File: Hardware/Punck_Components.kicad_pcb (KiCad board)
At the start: 4 copper layers, 91.2 x 99.8 mm, 115 parts, among them J1 Conn_01x12_Female, J2 Conn_01x12_Female, J3 Conn_01x12_Female, J4 Conn_01x12_Female, J5 Debug_Header, J6 SWD_Header, J7 Eurorack_10_pin_power, Q1 MMBT3904, Q2 MMBT3904, Q3 MMBT3904, Q4 MMBT3904, Q5 MMBT3904, Q6 MMBT3904, Q7 MMBT3904, U1 TL074, U2 STM32H743ZITx, U3 W25Q128JVS, U4 PCM5100APW, U5 W25Q128JVS, U6 TPS561201, U7 LD1117-3.3-4Tab, Y1 8MHz 20pF

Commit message: More PCB tweaking
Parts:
- moved R19 2.60 mm to (149.6, 119.6)
- moved R21 2.60 mm to (149.6, 122.2)
- moved R22 2.40 mm to (149.6, 124.8)
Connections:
- J2 pad 11: unconnected-(J2-Pad11) -> /TEMPO_OUT
- J4 pad 1: GND -> /USB_DP
- J4 pad 10: /TEMPO_OUT -> /AUDIO_OUT_L
- J4 pad 2: /USB_DP -> /USB_DM
- J4 pad 3: /USB_DM -> /USB_VBUS
- J4 pad 4: /USB_VBUS -> /KI_LED
- J4 pad 5: /KI_LED -> /SN_LED
- J4 pad 6: /SN_LED -> /HH_LED
- J4 pad 7: /HH_LED -> /SEQ_SELECT
- J4 pad 8: /SEQ_SELECT -> GND
- J4 pad 9: /AUDIO_OUT_L -> GND
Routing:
- net /TEMPO_OUT: track 31.4 -> 78.2 mm, vias 0 -> 1
- net /HH_LED_OUT: track 42.8 -> 41.3 mm
- net /USB_DP: track 43.9 -> 42.8 mm
- net /KI_LED_OUT: track 39.1 -> 38.0 mm
- net /SN_LED_OUT: track 40.7 -> 39.7 mm
- net /SEQ_SELECT: track 54.3 -> 53.2 mm
- net /AUDIO_OUT_L: track 44.6 -> 45.6 mm
- net /USB_DM: track 45.6 -> 44.6 mm
- net /USB_VBUS: track 47.5 -> 46.6 mm

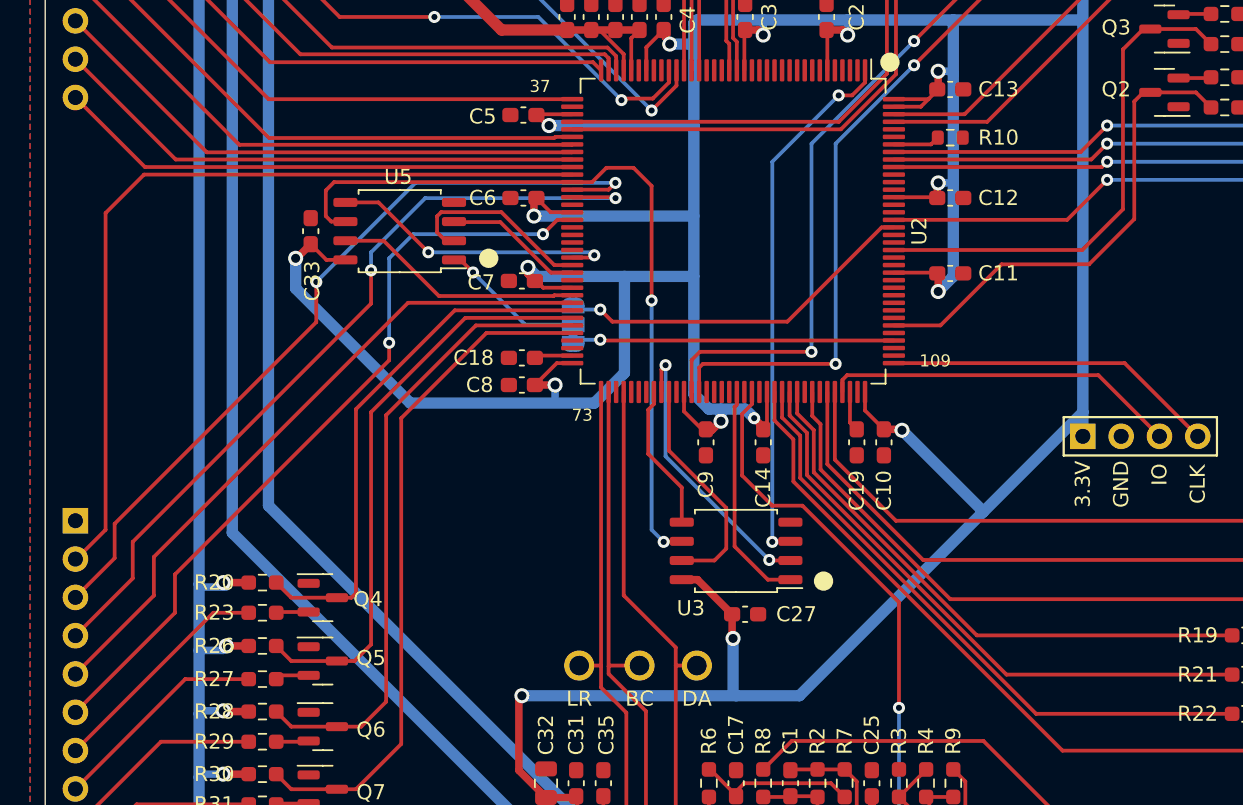
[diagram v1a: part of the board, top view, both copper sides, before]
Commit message: Added Logo to panel
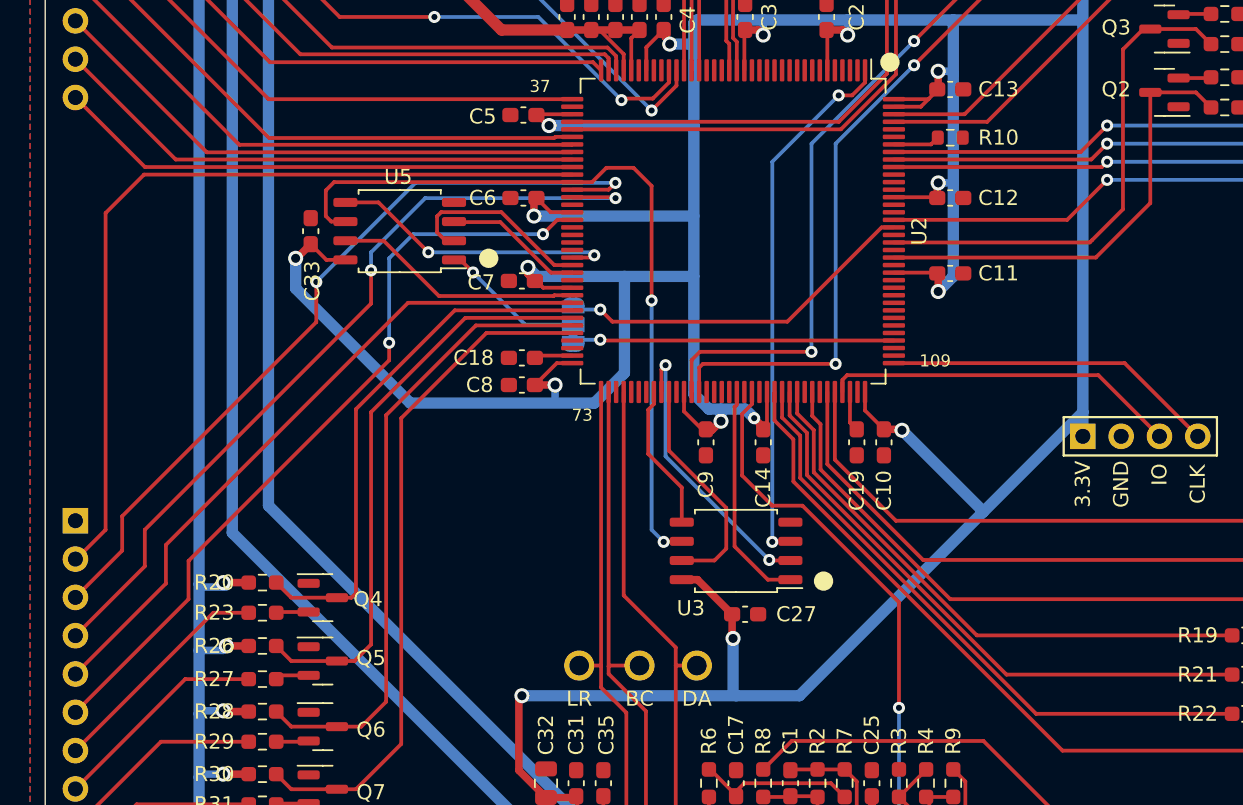
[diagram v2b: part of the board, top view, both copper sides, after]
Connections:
- U2 pad 114: /KICK_CLAMP -> unconnected-(U2-Pad114)
- U2 pad 123: unconnected-(U2-Pad123) -> /KICK_CLAMP
- U2 pad 124: /SNARE_CLAMP -> unconnected-(U2-Pad124)
- U2 pad 125: unconnected-(U2-Pad125) -> /SNARE_CLAMP
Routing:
- net /KICK_CLAMP: track 34.5 -> 32.4 mm

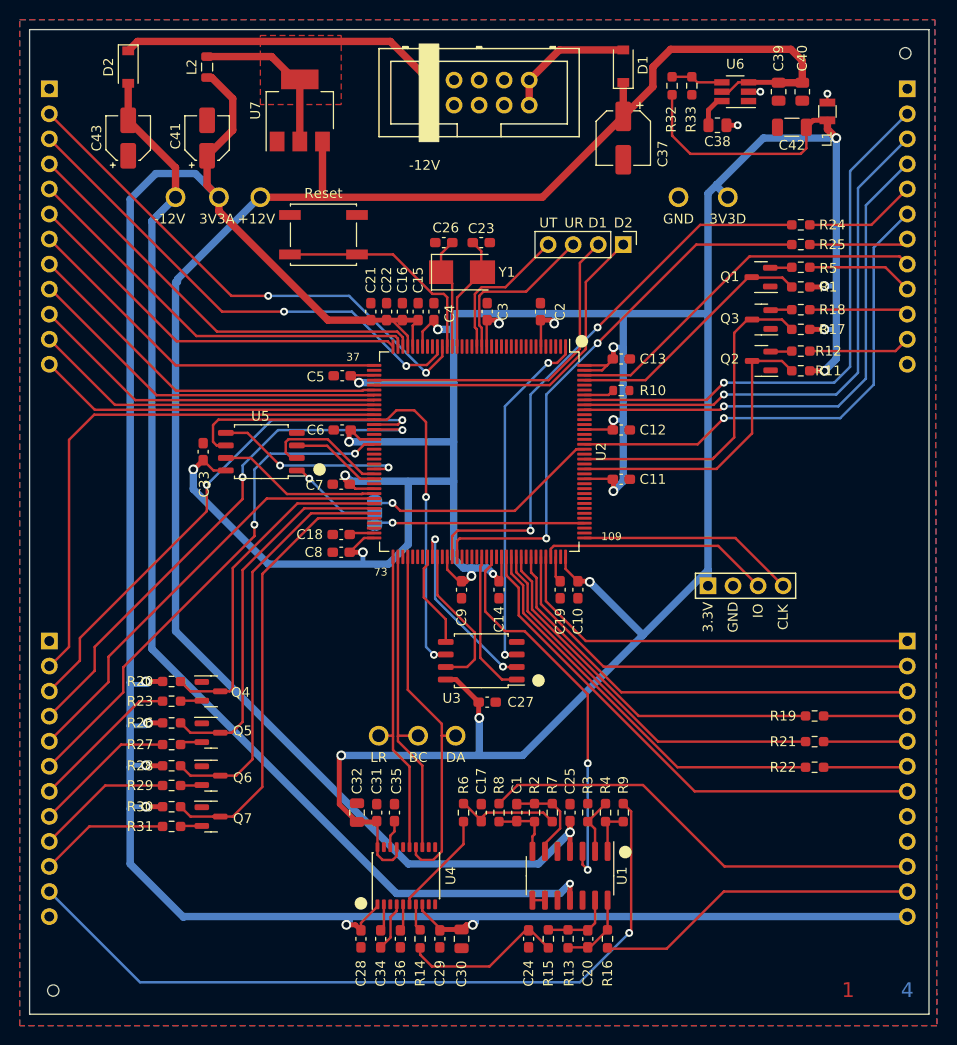
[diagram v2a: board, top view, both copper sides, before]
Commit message: More PCB tweaks; rejigged bottom row of controls
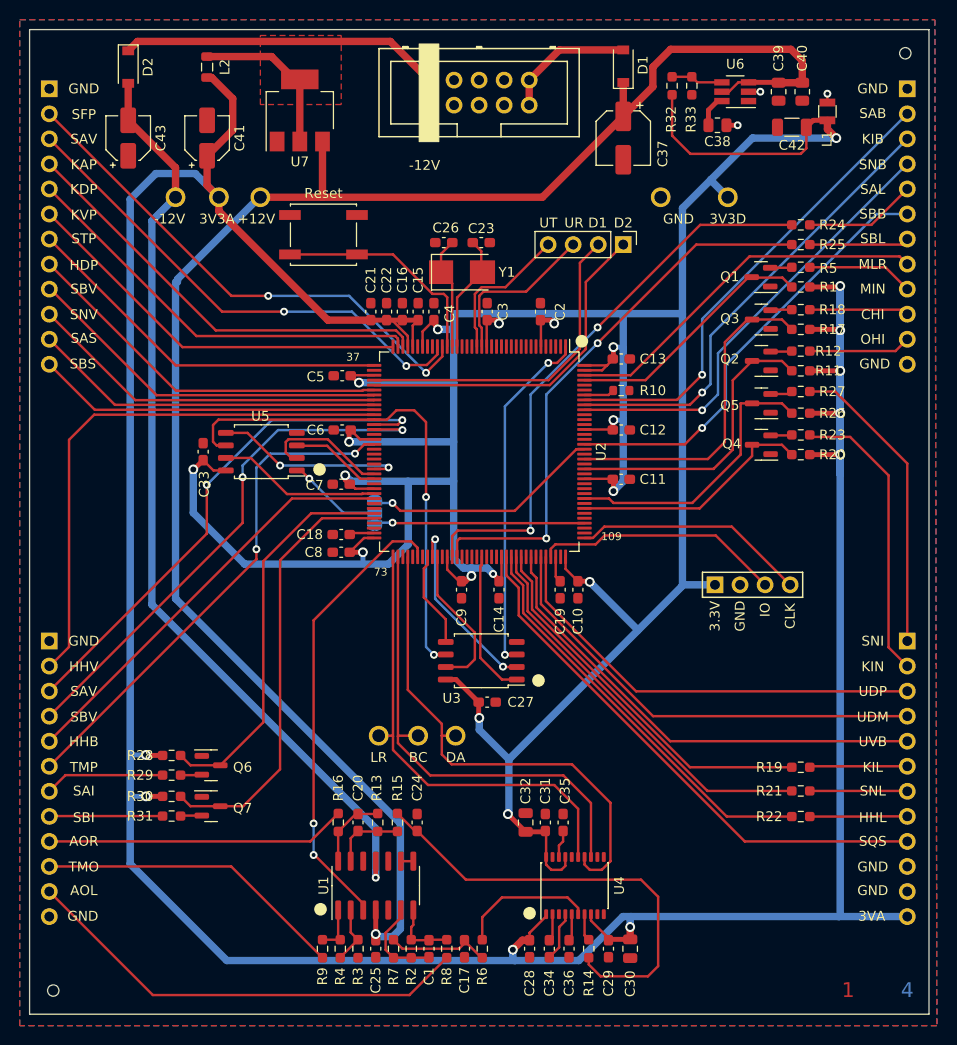
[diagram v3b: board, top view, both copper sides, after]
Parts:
- moved R27 73.2 mm to (148.2, 86.7), turned to 180 degrees
- moved R26 71.1 mm to (148.2, 88.9), turned to 0 degrees
- moved R23 69.3 mm to (148.2, 91.1), turned to 180 degrees
- moved R20 67.8 mm to (148.2, 93.1), turned to 0 degrees
- moved Q5 65.0 mm to (144.2, 87.9), turned to 180 degrees
- moved Q4 61.1 mm to (144.2, 92.1), turned to 180 degrees
- moved R9 33.5 mm to (99.7, 143.2), turned to -90 degrees
- moved R4 30.2 mm to (101.5, 143.2), turned to -90 degrees
- moved R16 29.7 mm to (101.3, 130.4), turned to 90 degrees
- moved R3 27.1 mm to (103.3, 143.2), turned to -90 degrees
- moved C20 26.1 mm to (103.3, 130.4), turned to -90 degrees
- moved C25 24.1 mm to (105.1, 143.2), turned to -90 degrees
- moved R13 22.6 mm to (105.3, 130.4), turned to -90 degrees
- moved R7 21.2 mm to (106.9, 143.2), turned to 90 degrees
- moved U1 19.7 mm to (105.1, 136.8), turned to 90 degrees
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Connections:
- J2 pad 10: /SAMPLER_B_IN -> /TEMPO_OUT
- J2 pad 11: /TEMPO_OUT -> /AUDIO_OUT_L
- J2 pad 7: /CH_IN -> /SAMPLER_A_IN
- J2 pad 8: /OH_IN -> /SAMPLER_B_IN
- J2 pad 9: /SAMPLER_A_IN -> /AUDIO_OUT_R
- J3 pad 10: /SNARE_IN -> /CH_IN
- J3 pad 11: /KICK_IN -> /OH_IN
- J4 pad 1: /USB_DP -> /SNARE_IN
- J4 pad 10: /AUDIO_OUT_L -> GND
- J4 pad 11: /AUDIO_OUT_R -> GND
- J4 pad 2: /USB_DM -> /KICK_IN
- J4 pad 3: /USB_VBUS -> /USB_DP
- J4 pad 4: /KI_LED -> /USB_DM
- J4 pad 5: /SN_LED -> /USB_VBUS
- J4 pad 6: /HH_LED -> /KI_LED
- J4 pad 7: /SEQ_SELECT -> /SN_LED
- J4 pad 8: GND -> /HH_LED
- J4 pad 9: GND -> /SEQ_SELECT
- Q2 pad 3: /KICK_CLAMP -> /OH_CLAMP
- Q3 pad 3: /SNARE_CLAMP -> /CH_CLAMP
- Q4 pad 3: /CH_CLAMP -> /KICK_CLAMP
- Q5 pad 3: /OH_CLAMP -> /SNARE_CLAMP
- R1 pad 2: +3V3 -> +3.3VA
- R11 pad 1: /KICK_CLAMP -> /OH_CLAMP
- R11 pad 2: +3V3 -> +3.3VA
- R12 pad 1: /KICK_IN -> /OH_IN
- R17 pad 1: /SNARE_CLAMP -> /CH_CLAMP
- R17 pad 2: +3V3 -> +3.3VA
- R18 pad 1: /SNARE_IN -> /CH_IN
- R20 pad 1: /CH_CLAMP -> /KICK_CLAMP
- R23 pad 1: /CH_IN -> /KICK_IN
- R26 pad 1: /OH_CLAMP -> /SNARE_CLAMP
- R27 pad 1: /OH_IN -> /SNARE_IN
- U2 pad 115: unconnected-(U2-Pad115) -> /KICK_CLAMP
- U2 pad 117: unconnected-(U2-Pad117) -> /SNARE_CLAMP
- U2 pad 123: /KICK_CLAMP -> /OH_CLAMP
- U2 pad 125: /SNARE_CLAMP -> /CH_CLAMP
- U2 pad 65: /CH_CLAMP -> unconnected-(U2-Pad65)
- U2 pad 66: /OH_CLAMP -> unconnected-(U2-Pad66)
- U2 pad 78: unconnected-(U2-Pad78) -> /TEMPO_CLOCK
- U2 pad 93: /TEMPO_CLOCK -> unconnected-(U2-Pad93)
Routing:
- net +3.3VA: track 234.0 -> 332.0 mm, vias 6 -> 9
- net /TEMPO_OUT: track 78.2 -> 31.5 mm, vias 1 -> 0
- net +3V3: track 398.2 -> 352.9 mm, vias 20 -> 17
- net Net-(C24-Pad1): track 16.4 -> 45.6 mm
- net /SNARE_IN: track 9.97 -> 30.9 mm
- net VEE: track 115.1 -> 94.6 mm
- net /KICK_IN: track 10.4 -> 29.8 mm
- net /DAC_BCLK: track 32.5 -> 48.5 mm
- net /DAC_LRCLK: track 31.6 -> 47.2 mm
- net /DAC_DATA: track 36.7 -> 51.9 mm
- net VCC: track 185.8 -> 175.3 mm
- net /SA_BTN: track 56.4 -> 48.1 mm
- net /KI_BTN: track 54.9 -> 46.8 mm
- net /SN_BTN: track 53.4 -> 45.6 mm
- net /KICK_CLAMP: track 32.4 -> 24.8 mm
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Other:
- board text added: "3VA"
- board text added: "AOL"
- board text added: "AOR"
- board text added: "CHI"
- board text added: "HDP"
- board text added: "HHB"
- board text added: "HHL"
- board text added: "HHV"
- board text added: "KAP"
- board text added: "KDP"
- board text added: "KIB"
- board text added: "KIL"
- board text added: "KIN"
- board text added: "KVP"
- board text added: "MIN"
- board text added: "MLR"
- board text added: "OHI"
- board text added: "SAB"
- board text added: "SAI"
- board text added: "SAL"
- board text added: "SAS"
- board text added: "SAV"
- board text added: "SBB"
- board text added: "SBI"
- board text added: "SBL"
- board text added: "SBS"
- board text added: "SBV"
- board text added: "SFP"
- board text added: "SNB"
- board text added: "SNI"
- board text added: "SNL"
- board text added: "SNV"
- board text added: "SQS"
- board text added: "STP"
- board text added: "TMO"
- board text added: "TMP"
- board text added: "UDM"
- board text added: "UDP"
- board text added: "UVB"

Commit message: Added test code to use PWM control on voice LEDs
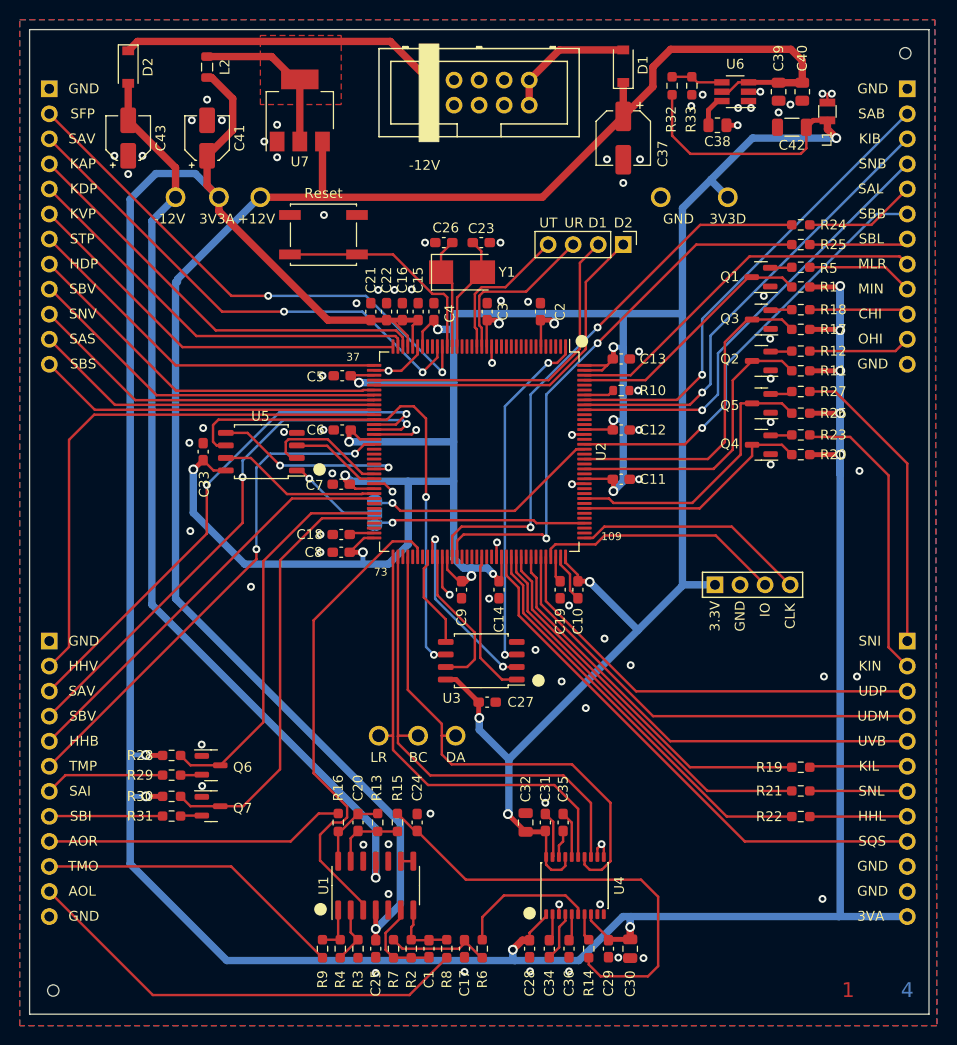
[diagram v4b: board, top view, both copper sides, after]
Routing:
- net GND: track 0.00 -> 40.7 mm, vias 0 -> 81
- net /TEMPO_CLOCK: track 46.6 -> 49.4 mm, vias 2 -> 0
- net /SAMPLER_B_VOL_POT: track 54.1 -> 56.1 mm
- net /SAMPLER_A_VOL_POT: track 53.1 -> 54.6 mm
- net VCC: track 175.3 -> 174.1 mm
- net /SNARE_FILTER_POT: track 52.4 -> 53.3 mm
- net /SAMPLER_A_VOICE_POT: track 50.2 -> 50.9 mm
- net /QSPI_CLK: track 51.0 -> 51.6 mm
- net /VSW: vias 3 -> 4

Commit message: Fixed incorrect pinout on transistors
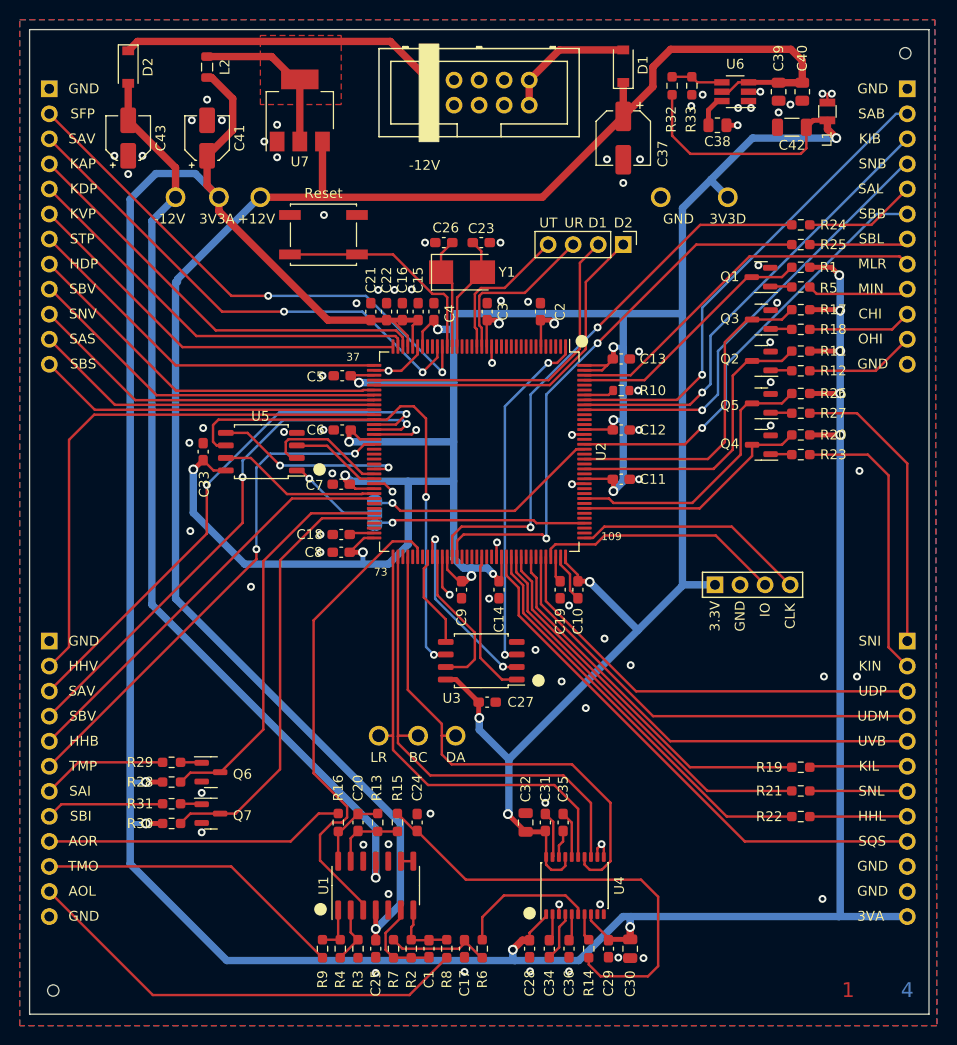
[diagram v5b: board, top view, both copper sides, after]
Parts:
- R19, R21, R22, R24, R25: value 1k -> 560
- R3: value 10k -> 15k
- R4: value 15k -> 10k
- moved R30 2.75 mm to (84.4, 130.5)
- moved R28 2.70 mm to (84.4, 126.3)
- moved R27 2.20 mm to (148.2, 88.9)
- moved R1 2.00 mm to (148.2, 74.1)
- moved R11 2.00 mm to (148.2, 82.6)
- moved R12 2.00 mm to (148.2, 84.6)
- moved R17 2.00 mm to (148.2, 78.4)
- moved R18 2.00 mm to (148.2, 80.4)
- moved R20 2.00 mm to (148.2, 91.1)
- moved R23 2.00 mm to (148.2, 93.1)
- moved R26 2.00 mm to (148.2, 86.9)
- moved R5 2.00 mm to (148.2, 76.1)
- moved R29 1.30 mm to (84.4, 124.3)
- moved R31 1.25 mm to (84.4, 128.5)
- moved Q7 0.75 mm to (88.4, 129.5)
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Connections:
- Q1 pad 1: GND -> Net-(Q1-Pad1)
- Q1 pad 2: Net-(Q1-Pad2) -> GND
- Q2 pad 1: GND -> Net-(Q2-Pad1)
- Q2 pad 2: Net-(Q2-Pad2) -> GND
- Q3 pad 1: GND -> Net-(Q3-Pad1)
- Q3 pad 2: Net-(Q3-Pad2) -> GND
- Q4 pad 1: GND -> Net-(Q4-Pad1)
- Q4 pad 2: Net-(Q4-Pad2) -> GND
- Q5 pad 1: GND -> Net-(Q5-Pad1)
- Q5 pad 2: Net-(Q5-Pad2) -> GND
- Q6 pad 1: GND -> Net-(Q6-Pad1)
- Q6 pad 2: Net-(Q6-Pad2) -> GND
- Q7 pad 1: GND -> Net-(Q7-Pad1)
- Q7 pad 2: Net-(Q7-Pad2) -> GND
- R12 pad 2: Net-(Q2-Pad2) -> Net-(Q2-Pad1)
- R18 pad 2: Net-(Q3-Pad2) -> Net-(Q3-Pad1)
- R23 pad 2: Net-(Q4-Pad2) -> Net-(Q4-Pad1)
- R27 pad 2: Net-(Q5-Pad2) -> Net-(Q5-Pad1)
- R29 pad 2: Net-(Q6-Pad2) -> Net-(Q6-Pad1)
- R31 pad 2: Net-(Q7-Pad2) -> Net-(Q7-Pad1)
- R5 pad 2: Net-(Q1-Pad2) -> Net-(Q1-Pad1)
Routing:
- net +3.3VA: track 332.0 -> 312.1 mm
- net Net-(Q5-Pad2): track 2.25 -> 0.00 mm
- net Net-(Q1-Pad2): track 2.21 -> 0.00 mm
- net Net-(Q1-Pad1): track 0.00 -> 2.21 mm
- net Net-(Q5-Pad1): track 0.00 -> 2.17 mm
- net Net-(Q4-Pad2): track 2.17 -> 0.00 mm
- net Net-(Q3-Pad1): track 0.00 -> 2.17 mm
- net Net-(Q2-Pad2): track 2.17 -> 0.00 mm
- net Net-(Q7-Pad2): track 2.17 -> 0.00 mm
- net Net-(Q4-Pad1): track 0.00 -> 2.17 mm
- net Net-(Q2-Pad1): track 0.00 -> 2.17 mm
- net Net-(Q6-Pad2): track 2.17 -> 0.00 mm
- net Net-(Q3-Pad2): track 2.17 -> 0.00 mm
- net Net-(Q6-Pad1): track 0.00 -> 2.16 mm
- net Net-(Q7-Pad1): track 0.00 -> 2.12 mm
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
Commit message: Final tweaking and v1 gerber creation; JLC order placed
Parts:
- removed H1, H2: JLC_Tooling_Hole, Custom_Footprints:JLC_SMT_Tooling_Hole
- added TP9: TestPoint, Custom_Footprints:1.3mm_Test_Point, F.Cu at (145.7, 146.6)
- moved J1 0.10 mm to (72.1, 56.0)
- moved J2 0.10 mm to (72.1, 112.0)
- moved J3 0.10 mm to (159.1, 56.0)
- moved J4 0.10 mm to (159.1, 112.0)
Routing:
- net GND: vias 81 -> 155
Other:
- board size 91.2 x 99.8 mm -> 91.2 x 100 mm
- board text added: "Mountjoy Modular Punck Components v1.0"
